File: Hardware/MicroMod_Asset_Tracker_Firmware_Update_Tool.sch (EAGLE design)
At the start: 26 parts, among them J5 MICROMOD-2222, U2 CH340G, Y1 12MHz

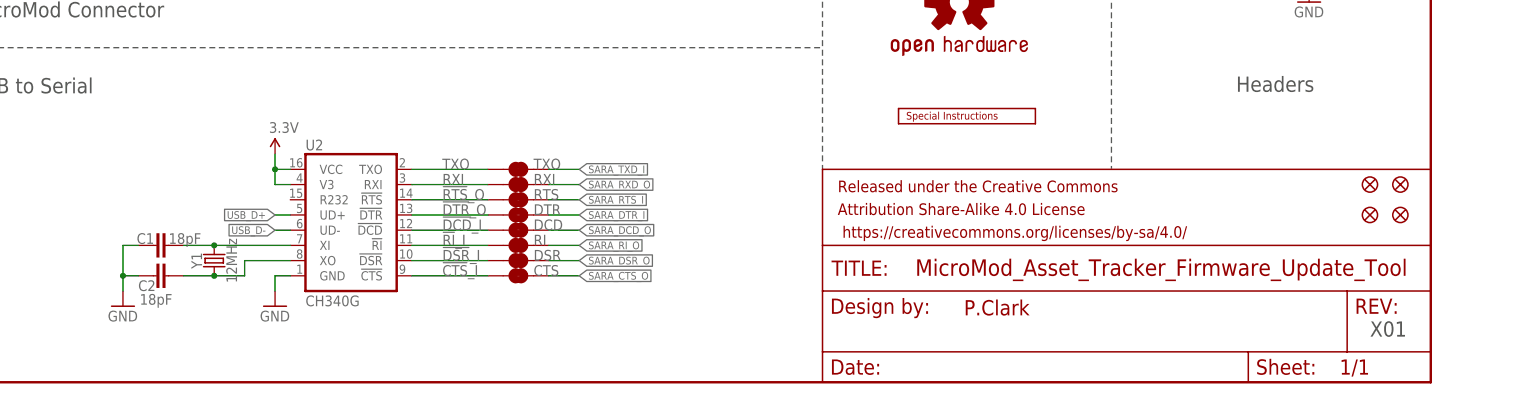
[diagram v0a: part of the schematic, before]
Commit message: Changed to the CH340C
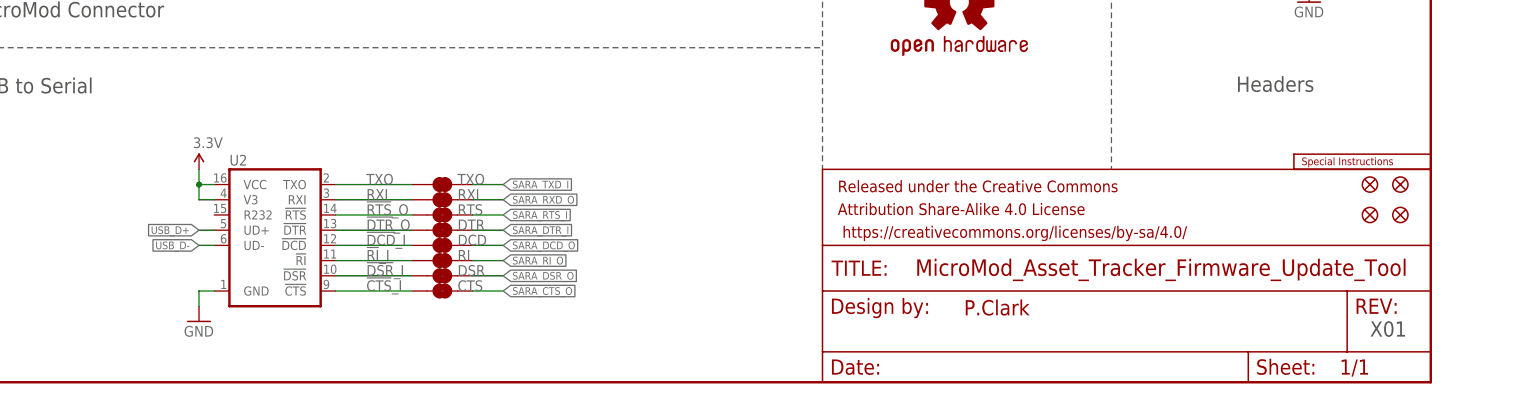
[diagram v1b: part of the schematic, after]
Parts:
- removed C1, C2: 18pF, SparkFun-Capacitors:18PF-0603-50V-5%
- removed Y1: 12MHz, SparkFun-Clocks:CRYSTAL-12MHZ"
- U2: value CH340G -> CH340C; device SparkFun-IC-Comms:CH340GSMD -> SparkFun-IC-Comms:CH340C
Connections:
- removed net N$1: C2.2, U2.XO, Y1.1
- removed net N$2: C1.2, U2.XI, Y1.2
- net GND: no longer C1.1, C2.1
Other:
- moved on the sheet: CTS, DCD, DSR, DTR, RI, RTS, RXI, TXO

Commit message: Updates for v10
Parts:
- removed SPARKX2: SPARKX-LOGO4, SparkX:SPARKX-LOGO4
- added LOGO3: SFE_LOGO_NAME_FLAME.1_INCH, SparkFun-Aesthetics:SFE_LOGO_NAME_FLAME.1_INCH
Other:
- note added: "v10"
- note removed: "X01"
- moved on the sheet: CTS, DCD, DSR, DTR, J1, J2, RI, RTS, RXI, TXO, U2
